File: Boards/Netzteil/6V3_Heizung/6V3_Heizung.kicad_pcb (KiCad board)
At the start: 2 copper layers, 100 x 80 mm, 64 parts, among them P1 7V5_AC, P2 12V_DC, P3 6V3_DC_1, P4 6V3_DC_2, P5 Relais, Q1 IRF540N, Q2 IRF540N, Q3 BS170, U1 TL072, U2 LM393

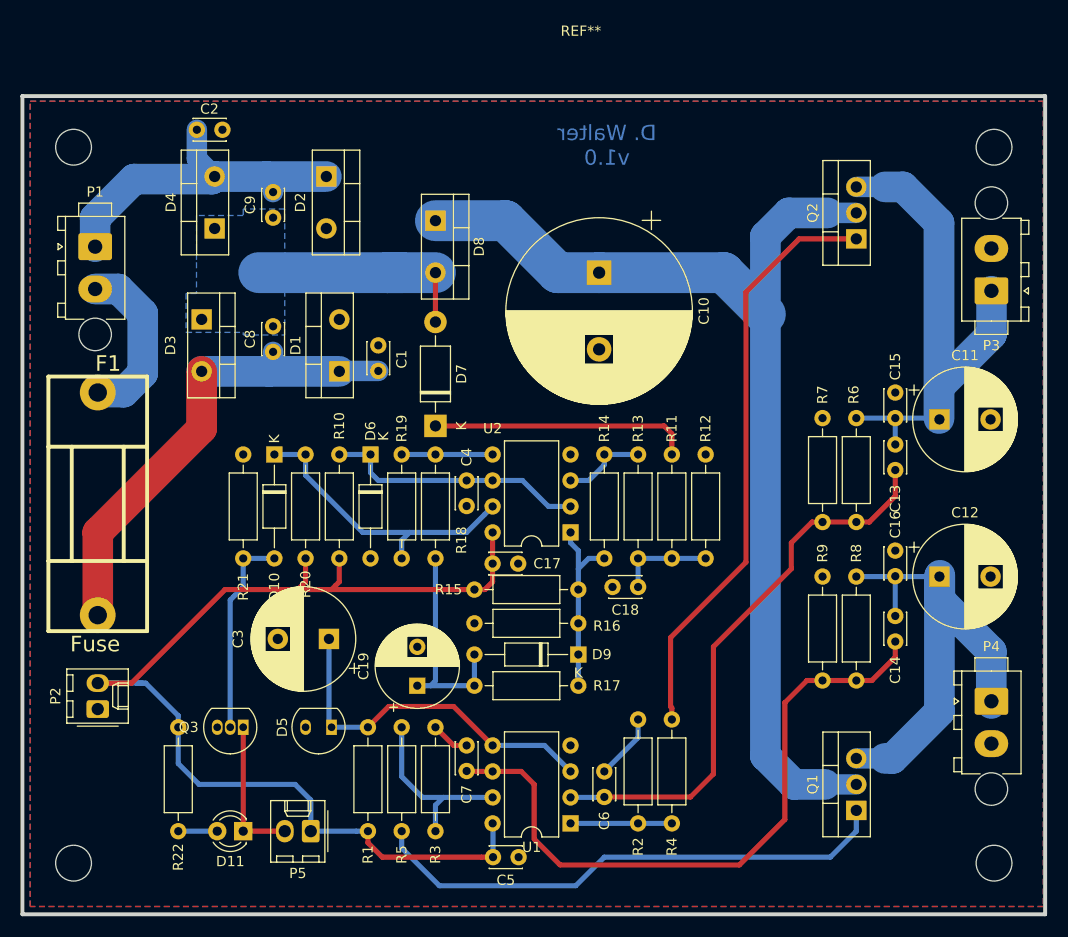
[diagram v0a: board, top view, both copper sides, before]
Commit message: Added Vias & Mounting Holes
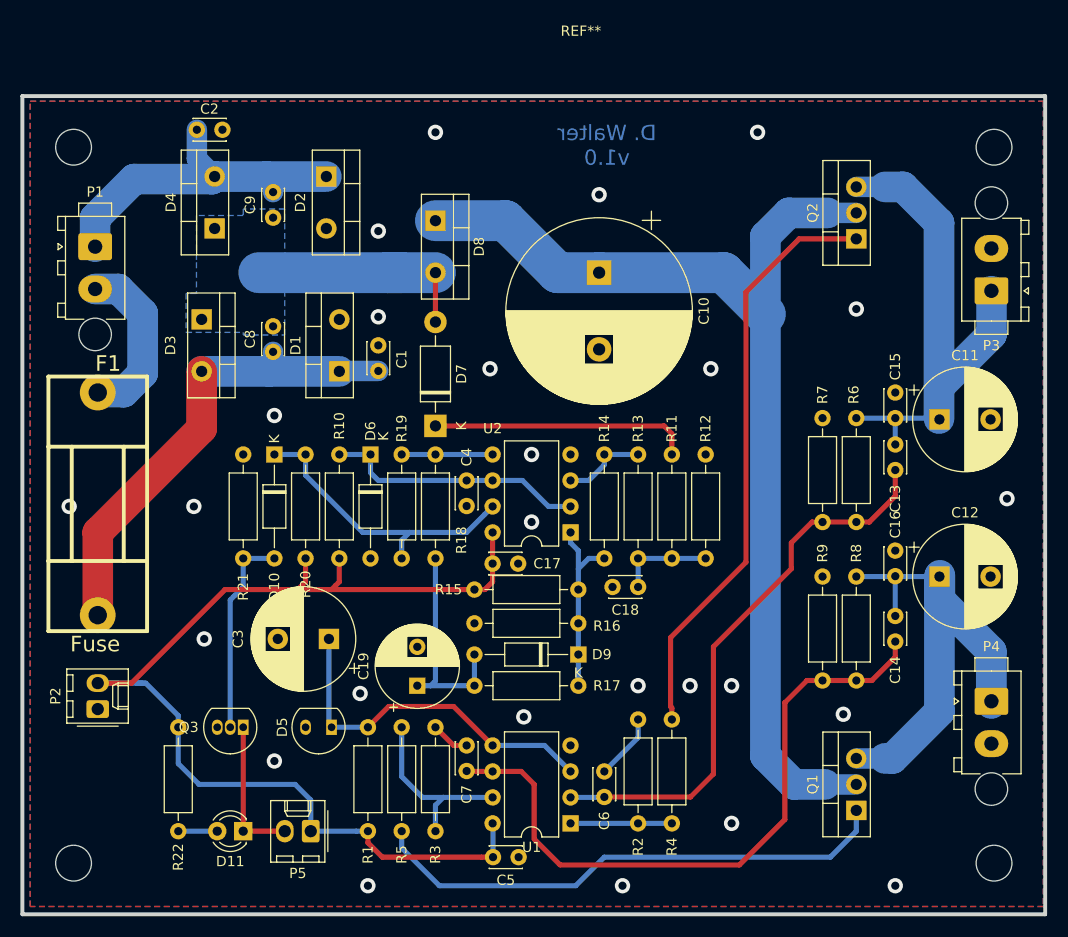
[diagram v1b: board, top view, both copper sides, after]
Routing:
- net GND: vias 0 -> 26
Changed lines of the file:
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@@
     (thickness 1.6)
     (drawings 1)
-    (tracks 214)
+    (tracks 240)
     (zones 0)
     (modules 64)
@@
   )
   (setup
-    (last_trace_width 0.5)
+    (last_trace_width 0.25)
     (user_trace_width 0.5)
     (user_trace_width 1)
@@
   (segment (start 66.929 89.6239) (end 66.929 81.534) (width 3) (layer F.Cu) (net 1))
   (segment (start 66.929 81.534) (end 77.089 71.374) (width 3) (layer F.Cu) (net 1))
+  (via (at 119.761 96.52) (size 1.5) (drill 0.8) (layers F.Cu B.Cu) (net 2))
+  (via (at 124.841 96.52) (size 1.5) (drill 0.8) (layers F.Cu B.Cu) (net 2))
+  (via (at 128.905 96.52) (size 1.5) (drill 0.8) (layers F.Cu B.Cu) (net 2))
+  (via (at 92.583 97.282) (size 1.5) (drill 0.8) (layers F.Cu B.Cu) (net 2))
+  (via (at 76.327 78.994) (size 1.5) (drill 0.8) (layers F.Cu B.Cu) (net 2))
+  (via (at 94.361 60.452) (size 1.5) (drill 0.8) (layers F.Cu B.Cu) (net 2))
+  (via (at 94.361 52.07) (size 1.5) (drill 0.8) (layers F.Cu B.Cu) (net 2))
+  (via (at 105.283 65.532) (size 1.5) (drill 0.8) (layers F.Cu B.Cu) (net 2))
+  (via (at 109.347 73.914) (size 1.5) (drill 0.8) (layers F.Cu B.Cu) (net 2))
+  (via (at 109.347 80.518) (size 1.5) (drill 0.8) (layers F.Cu B.Cu) (net 2))
+  (via (at 108.585 99.568) (size 1.5) (drill 0.8) (layers F.Cu B.Cu) (net 2))
+  (via (at 126.873 65.532) (size 1.5) (drill 0.8) (layers F.Cu B.Cu) (net 2))
+  (via (at 115.951 48.514) (size 1.5) (drill 0.8) (layers F.Cu B.Cu) (net 2))
+  (via (at 141.097 59.69) (size 1.5) (drill 0.8) (layers F.Cu B.Cu) (net 2))
+  (via (at 155.829 78.232) (size 1.5) (drill 0.8) (layers F.Cu B.Cu) (net 2))
+  (via (at 144.907 116.078) (size 1.5) (drill 0.8) (layers F.Cu B.Cu) (net 2))
+  (via (at 139.827 99.314) (size 1.5) (drill 0.8) (layers F.Cu B.Cu) (net 2))
+  (via (at 128.905 109.982) (size 1.5) (drill 0.8) (layers F.Cu B.Cu) (net 2))
+  (via (at 84.201 103.886) (size 1.5) (drill 0.8) (layers F.Cu B.Cu) (net 2))
+  (via (at 99.949 42.418) (size 1.5) (drill 0.8) (layers F.Cu B.Cu) (net 2))
+  (via (at 131.445 42.418) (size 1.5) (drill 0.8) (layers F.Cu B.Cu) (net 2))
+  (via (at 64.135 78.994) (size 1.5) (drill 0.8) (layers F.Cu B.Cu) (net 2))
+  (via (at 84.201 70.104) (size 1.5) (drill 0.8) (layers F.Cu B.Cu) (net 2))
+  (via (at 118.237 116.078) (size 1.5) (drill 0.8) (layers F.Cu B.Cu) (net 2))
+  (via (at 93.345 116.078) (size 1.5) (drill 0.8) (layers F.Cu B.Cu) (net 2))
+  (via (at 77.343 91.948) (size 1.5) (drill 0.8) (layers F.Cu B.Cu) (net 2))
   (segment (start 76.621 44.998) (end 78.359 46.736) (width 2) (layer B.Cu) (net 3) (status 20))
   (segment (start 76.621 42.164) (end 76.621 44.998) (width 2) (layer B.Cu) (net 3) (status 10))

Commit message: Added Test, moved mounting holes
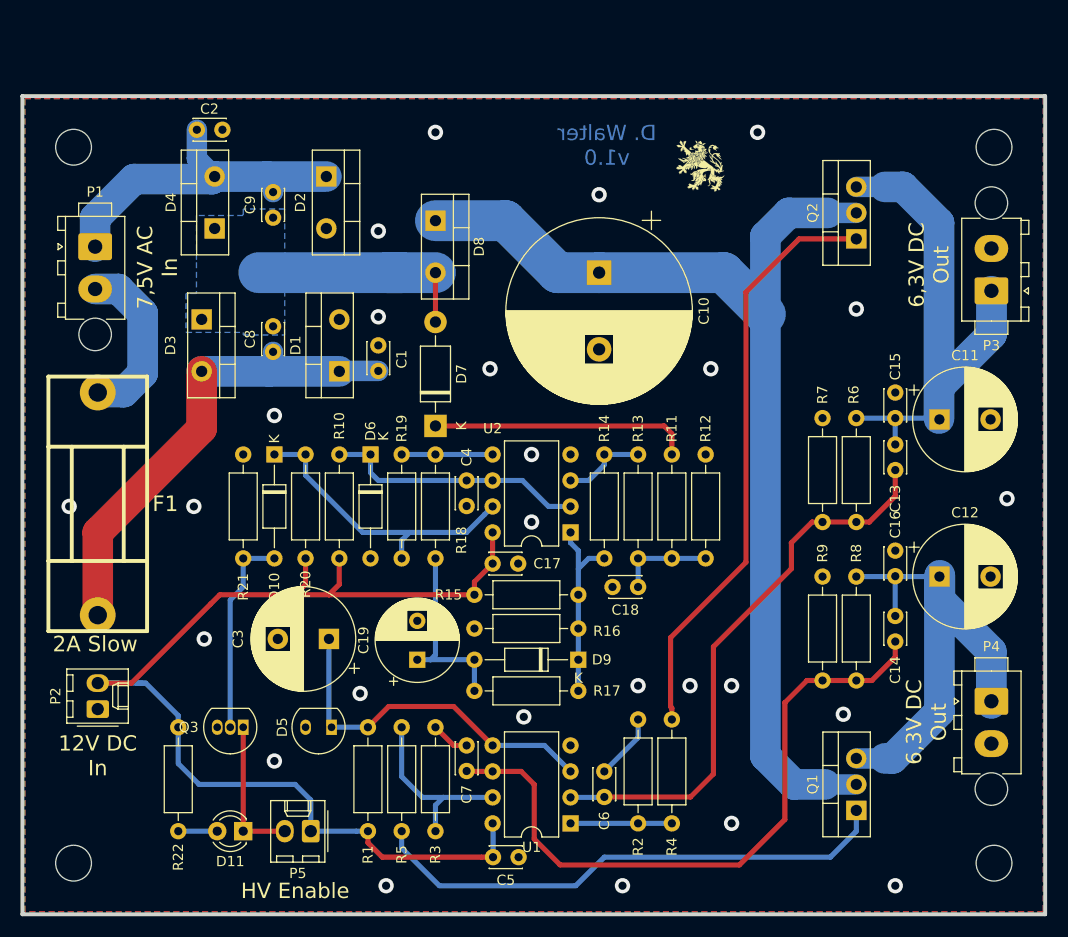
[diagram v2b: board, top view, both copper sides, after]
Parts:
- added G***: LOGO, Loewe:Loewe_Klein, F.Cu at (125.9, 45.7)
- F1: value Fuse -> 2A Slow
- moved C19 2.54 mm to (98.2, 94.0)
- moved D9 0.51 mm to (113.9, 94.0)
- moved R17 0.51 mm to (113.9, 97.0)
- moved R15 0.51 mm to (113.9, 87.6)
- moved R16 0.51 mm to (103.8, 90.9)
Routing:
- net Net-(C19-Pad1): track 21.3 -> 18.7 mm
- net +12V: track 111.1 -> 112.1 mm
- net Net-(D9-Pad1): track 18.3 -> 18.8 mm
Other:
- board text added: "12V DC In"
- board text added: "6,3V DC Out"
- board text added: "7,5V AC In"
- board text added: "HV Enable"
